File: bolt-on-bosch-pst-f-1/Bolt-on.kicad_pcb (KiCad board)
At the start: 4 copper layers, 42 x 72 mm, 12 parts

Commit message: cleanup kicad design
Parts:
- removed R_PRESS_BOT: ﻿10kΩ, Resistor_SMD:R_0805_2012Metric_Pad1.20x1.40mm_HandSolder
- removed R_PRESS_TOP: ﻿5.6kΩ, Resistor_SMD:R_0805_2012Metric_Pad1.20x1.40mm_HandSolder
- R_PRESS_BOT1, R_PRESS_TOP1: moved to B.Cu
- moved R_PRESS_BOT1 170.4 mm to (143.0, 96.5), turned to 90 degrees
- moved R_PRESS_TOP1 165.0 mm to (138.5, 96.5), turned to 90 degrees
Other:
- board text added: "5V"
- board text added: "CAN2H"
- board text added: "CAN2L"
- board text added: "GND"
- board text added: "PRESS_SIG"
- board text added: "TEMP_SIG"

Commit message: update readme
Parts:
- removed JPST-F_1_IN1: Conn_01x04, Connector_JST:JST_PH_S4B-PH-K_1x04_P2.00mm_Horizontal
- added PST-F1_IN1: Conn_01x04, Connector_JST:JST_PH_S4B-PH-K_1x04_P2.00mm_Horizontal, B.Cu at (136.5, 76.0)
- moved C2 16.0 mm to (143.5, 84.5), turned to 0 degrees
- moved C1 9.39 mm to (143.5, 88.0), turned to 0 degrees
- moved CAN2_5V1 1.50 mm to (153.5, 76.0)
- moved D1 0.71 mm to (159.0, 96.5)
- moved R_PRESS_BOT1 0.50 mm to (142.5, 96.5)
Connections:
- C1 pad 2: IO35 -> /IO35
- C2 pad 2: IO36 -> /IO36
- D1 pad 1: unconnected-(D1-Pad1) -> /IO35
- D1 pad 2: IO35 -> /IO36
- R_PRESS_BOT1 pad 1: IO35 -> /IO35
- R_PRESS_TOP1 pad 1: IO35 -> /IO35
- R_TEMP_TOP1 pad 1: IO36 -> /IO36
- SV1 pad 12: IO35 -> /IO35
- SV1 pad 13: IO36 -> /IO36
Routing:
- net /IO36: track 0.00 -> 79.0 mm
- net IO36: track 76.0 -> 0.00 mm
- net /IO35: track 0.00 -> 51.0 mm
- net IO35: track 39.9 -> 0.00 mm
- net GND: track 90.1 -> 77.6 mm
- net /+5V: track 81.0 -> 85.0 mm
- net /CAN2H: track 33.0 -> 34.9 mm
- net Net-(PST-F1_IN1-PRESS_SIG): track 18.0 -> 19.5 mm
- net /CAN2L: track 31.3 -> 30.3 mm

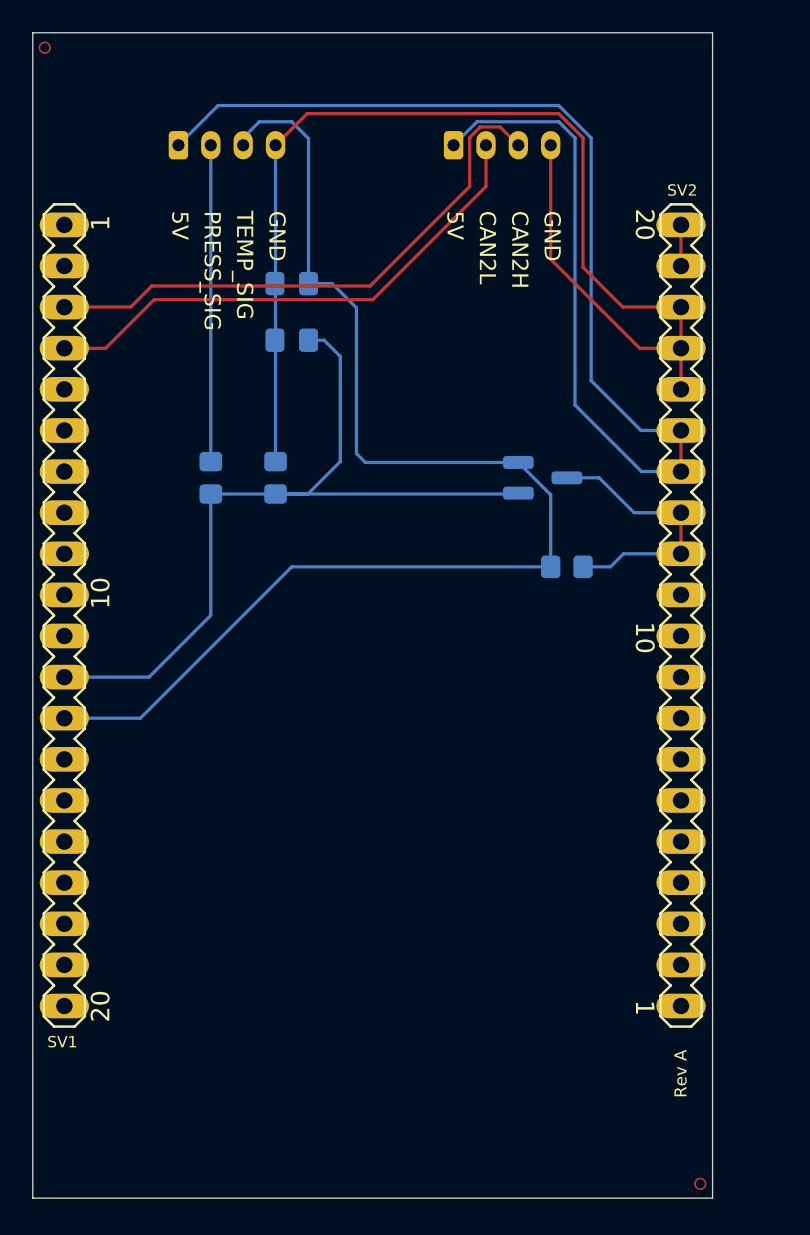
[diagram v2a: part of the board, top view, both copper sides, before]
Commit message: add copper pour to gnd and 5v
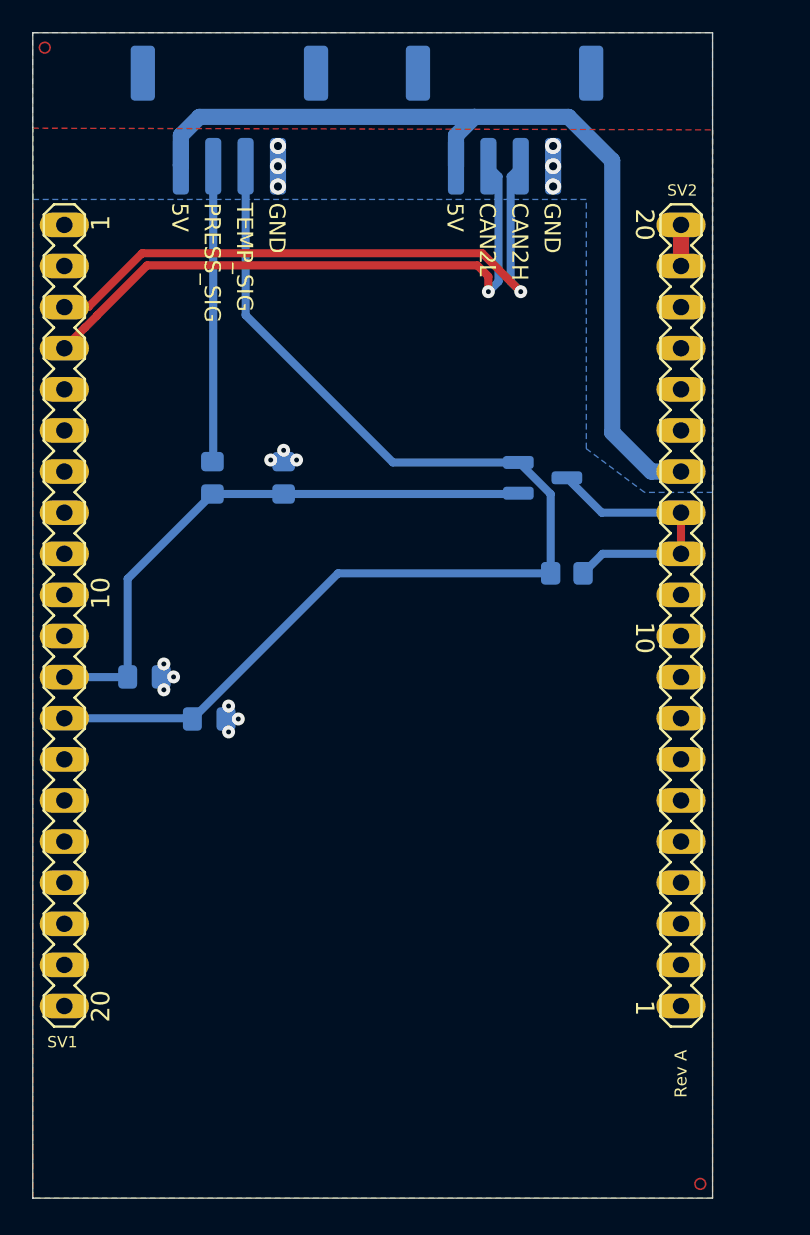
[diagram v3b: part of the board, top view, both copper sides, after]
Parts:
- CAN2_5V1, PST-F1_IN1: footprint Connector_JST:JST_PH_S4B-PH-K_1x04_P2.00mm_Horizontal -> Connector_JST:JST_PH_S4B-PH-SM4-TB_1x04-1MP_P2.00mm_Horizontal
- moved C2 27.4 mm to (138.4, 111.4), turned to 180 degrees
- moved C1 22.7 mm to (134.4, 108.8), turned to 180 degrees
- moved CAN2_5V1 3.51 mm to (156.7, 74.4)
- moved PST-F1_IN1 3.51 mm to (139.7, 74.4)
- moved R_PRESS_BOT1 0.50 mm to (143.0, 96.5)
- moved R_TEMP_TOP1 0.40 mm to (160.5, 102.4)
- moved R_PRESS_TOP1 0.10 mm to (138.6, 96.5)
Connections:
- net /CAN2H renamed /CAN2+
- net /CAN2L renamed /CAN2-
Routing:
- net GND: track 77.6 -> 0.00 mm, vias 0 -> 15
- net /+5V: track 85.0 -> 55.7 mm
- net /IO35: track 51.0 -> 36.6 mm
- net /IO36: track 79.0 -> 71.3 mm
- net /CAN2-: track 30.3 -> 37.9 mm, vias 0 -> 1
- net /CAN2+: track 34.9 -> 38.8 mm, vias 0 -> 1
- net Net-(PST-F1_IN1-PRESS_SIG): track 19.5 -> 18.3 mm
- added copper zone on B.Cu, net /+5V
- added copper zone on F.Cu, net GND

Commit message: swaped jst positions
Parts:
- added C3: ﻿0.1µF, Capacitor_SMD:C_0805_2012Metric_Pad1.18x1.45mm_HandSolder, B.Cu at (151.6, 81.5)
- added C4: 1µF, Capacitor_SMD:C_0805_2012Metric_Pad1.18x1.45mm_HandSolder, B.Cu at (148.4, 81.5)
- added C5: 10µF, Capacitor_SMD:C_1206_3216Metric_Pad1.33x1.80mm_HandSolder, B.Cu at (145.0, 81.5)
- moved CAN2_5V1 17.0 mm to (139.7, 74.1)
- moved PST-F1_IN1 17.0 mm to (156.7, 74.1)
- moved C2 4.26 mm to (134.3, 112.4)
- moved C1 1.11 mm to (134.3, 107.7)
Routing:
- net GND: track 0.00 -> 24.9 mm, vias 15 -> 8
- net /CAN2+: track 38.8 -> 23.1 mm
- net /CAN2-: track 37.9 -> 22.2 mm
- net Net-(PST-F1_IN1-PRESS_SIG): track 18.3 -> 32.7 mm
- net /IO36: track 71.3 -> 61.0 mm
- net /IO35: track 36.6 -> 35.8 mm

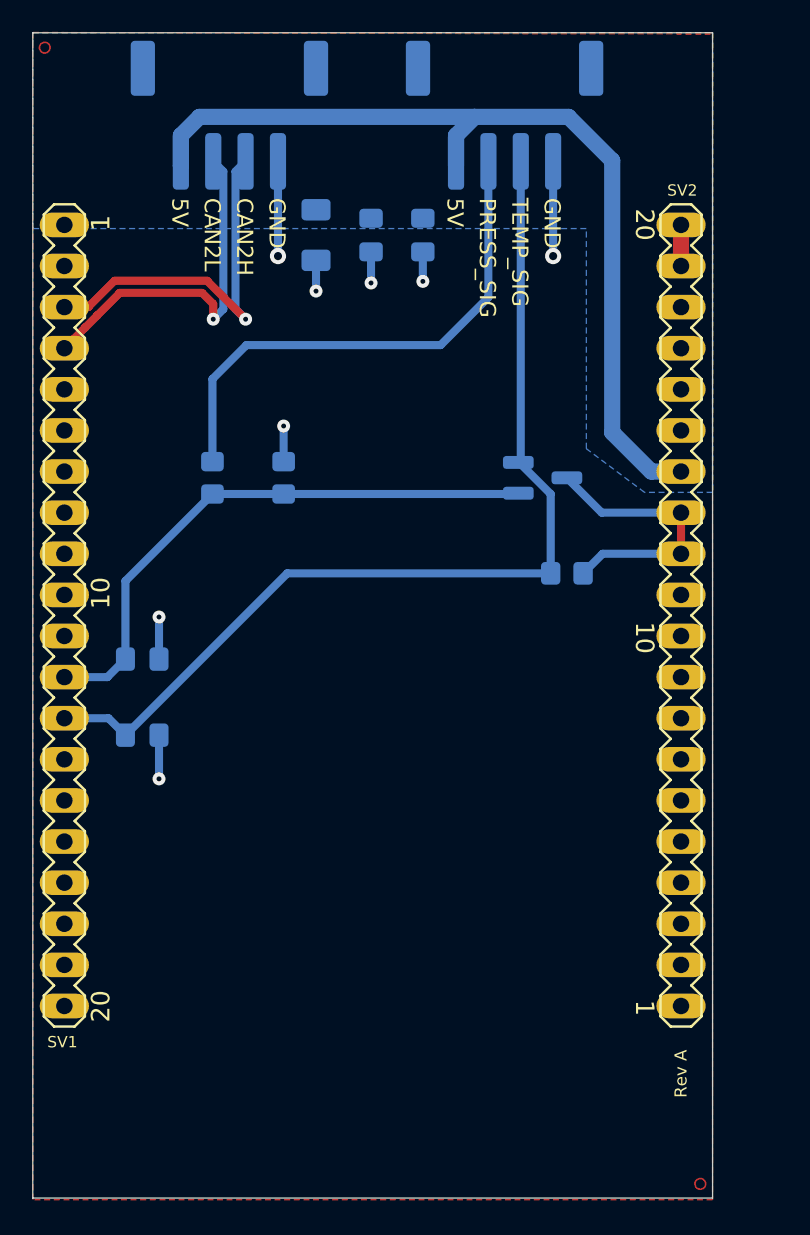
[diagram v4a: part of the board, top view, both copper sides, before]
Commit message: redo board layout
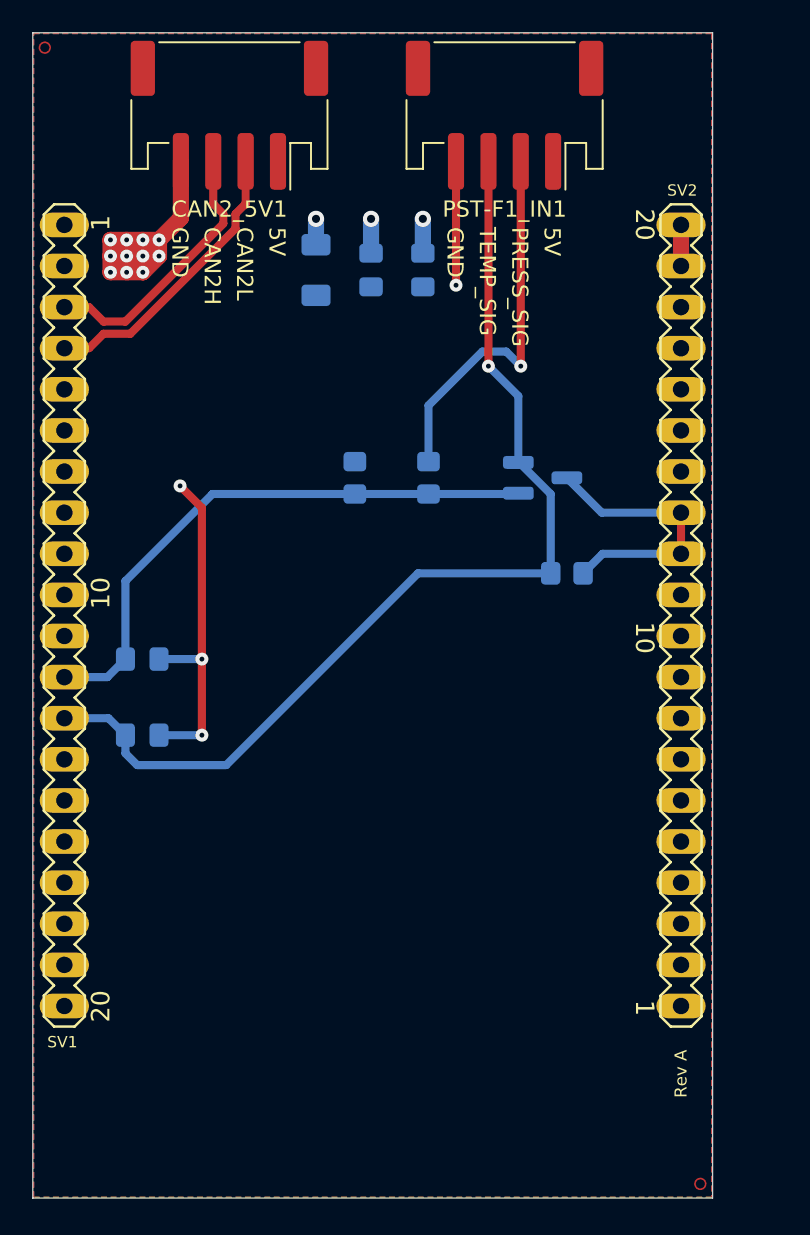
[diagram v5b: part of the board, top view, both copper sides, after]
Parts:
- CAN2_5V1, PST-F1_IN1: moved to F.Cu
- moved R_PRESS_TOP1 13.3 mm to (151.9, 96.5)
- moved R_PRESS_BOT1 4.40 mm to (147.4, 96.5)
- moved C3 2.16 mm to (151.6, 83.7)
- moved C4 2.16 mm to (148.4, 83.7)
- moved C5 2.16 mm to (145.0, 83.7)
- turned CAN2_5V1 to 180 degrees
- turned PST-F1_IN1 to 180 degrees
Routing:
- net /+5V: track 55.7 -> 5.85 mm, vias 0 -> 3
- net GND: track 24.9 -> 50.7 mm, vias 8 -> 15
- net Net-(PST-F1_IN1-PRESS_SIG): track 32.7 -> 23.6 mm, vias 0 -> 1
- net /CAN2+: track 23.1 -> 16.8 mm, vias 1 -> 0
- net /CAN2-: track 22.2 -> 18.1 mm, vias 1 -> 0
- net /IO36: track 61.0 -> 64.1 mm, vias 0 -> 1
- added copper zone on F.Cu, net /+5V
- added copper zone on B.Cu, net GND
- removed copper zone on B.Cu, net /+5V
- removed copper zone on F.Cu, net GND
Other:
- copper layers 4 -> 2

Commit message: update board layout
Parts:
- moved R_TEMP_TOP1 25.3 mm to (137.7, 113.3)
- moved D1 15.2 mm to (146.7, 105.4)
- moved R_PRESS_BOT1 12.5 mm to (137.0, 103.5)
- moved R_PRESS_TOP1 12.5 mm to (141.5, 103.5)
- moved C1 1.38 mm to (133.7, 106.4), turned to -90 degrees
- moved C2 0.55 mm to (133.7, 112.3), turned to -90 degrees
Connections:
- D1 pad 1: /IO35 -> /IO36
- D1 pad 2: /IO36 -> /IO35
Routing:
- net /+3.3V: track 17.0 -> 58.6 mm
- net /IO35: track 35.8 -> 17.5 mm
- net GND: track 50.7 -> 35.0 mm, vias 15 -> 16
- net Net-(PST-F1_IN1-PRESS_SIG): track 23.6 -> 37.7 mm
- net /IO36: track 64.1 -> 56.1 mm

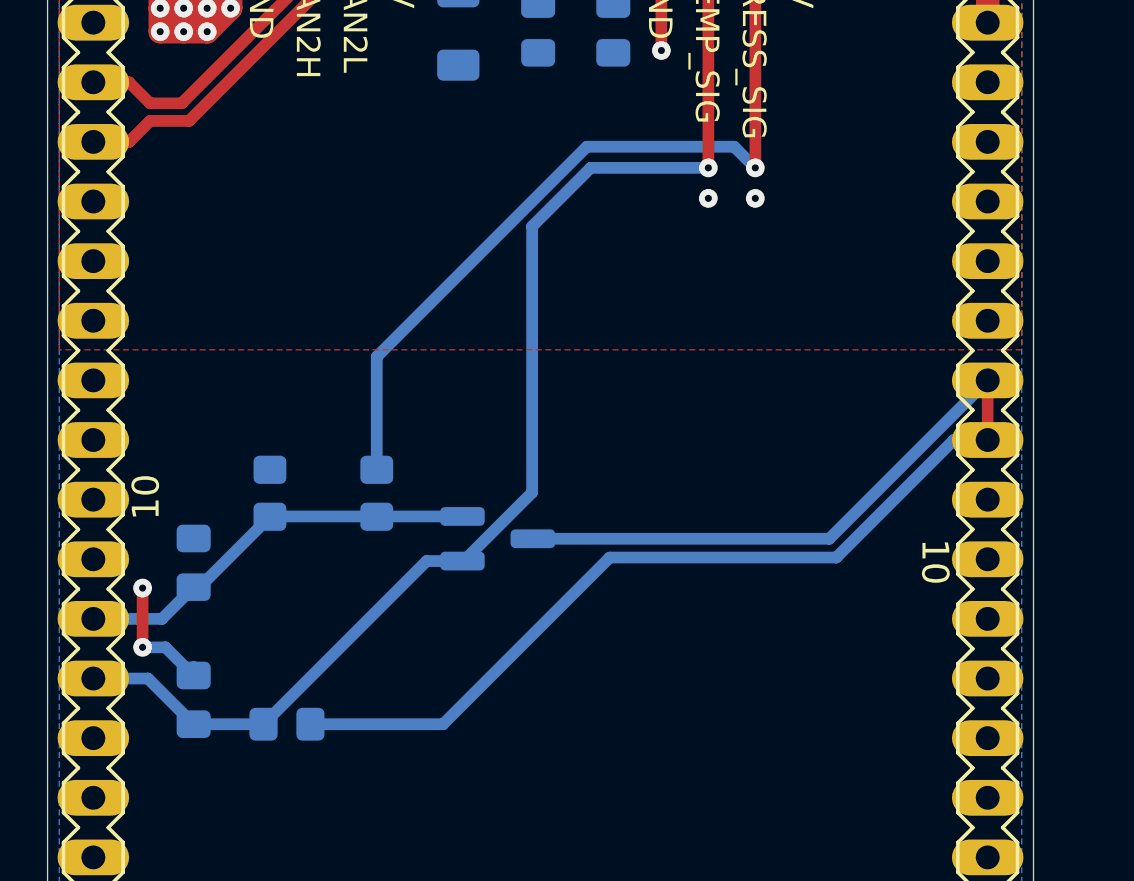
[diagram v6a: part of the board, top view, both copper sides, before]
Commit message: added low diode for proper clamp
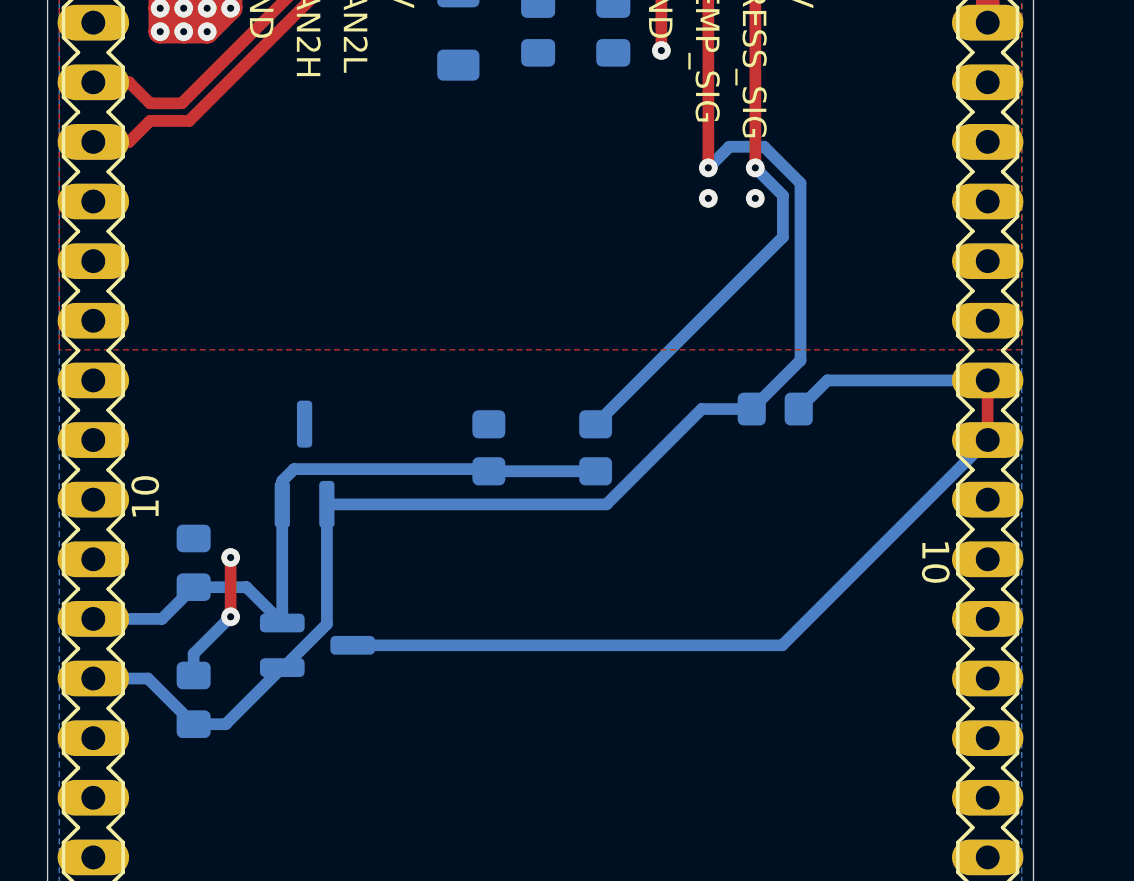
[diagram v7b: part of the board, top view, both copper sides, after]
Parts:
- added D2: BAT54A, Package_TO_SOT_SMD:TSOT-23_HandSoldering, B.Cu at (138.4, 102.2)
- moved R_TEMP_TOP1 24.8 mm to (158.5, 99.9)
- moved R_PRESS_BOT1 9.52 mm to (146.3, 101.5)
- moved R_PRESS_TOP1 9.52 mm to (150.8, 101.5)
- moved D1 8.92 mm to (139.0, 109.9)
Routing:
- net /+3.3V: track 58.6 -> 41.8 mm
- net /IO35: track 17.5 -> 29.2 mm
- net Net-(PST-F1_IN1-PRESS_SIG): track 37.7 -> 27.4 mm
- net /IO36: track 56.1 -> 65.4 mm

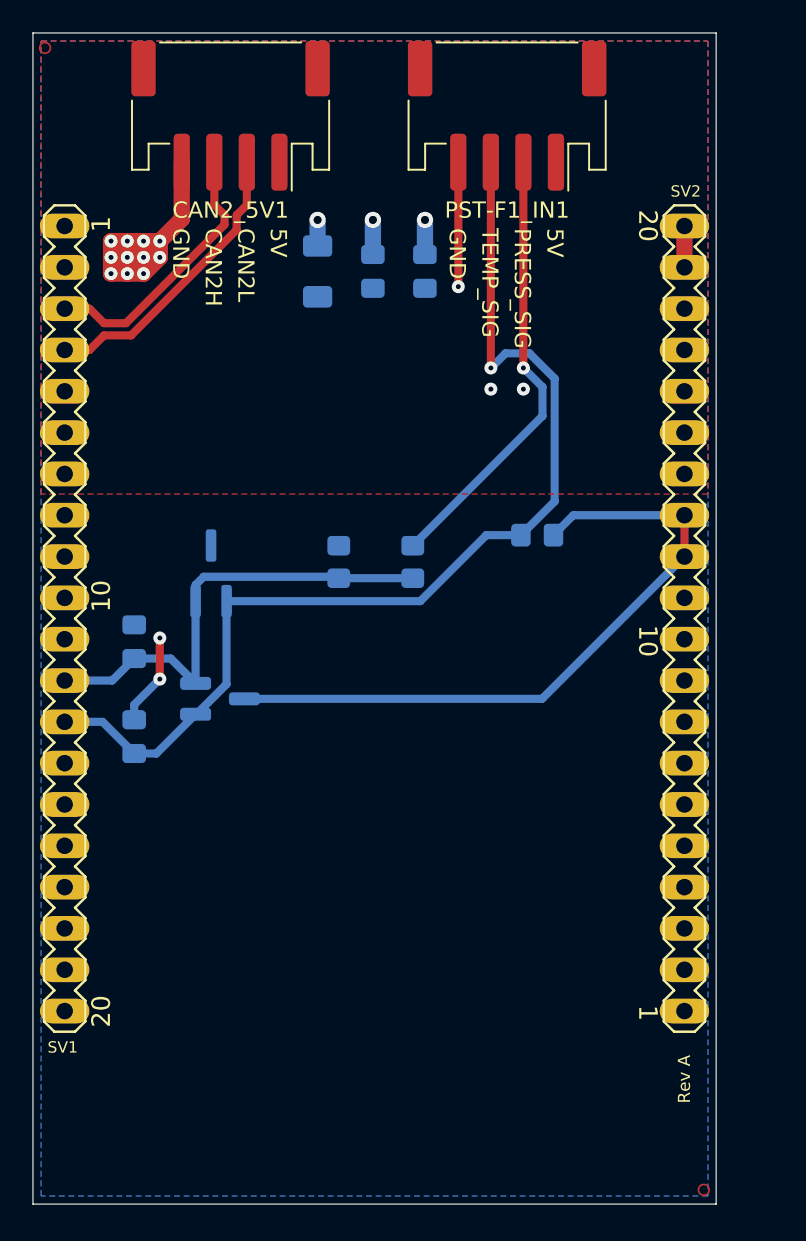
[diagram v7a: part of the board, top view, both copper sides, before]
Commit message: pcb add ground copper pour on both sides
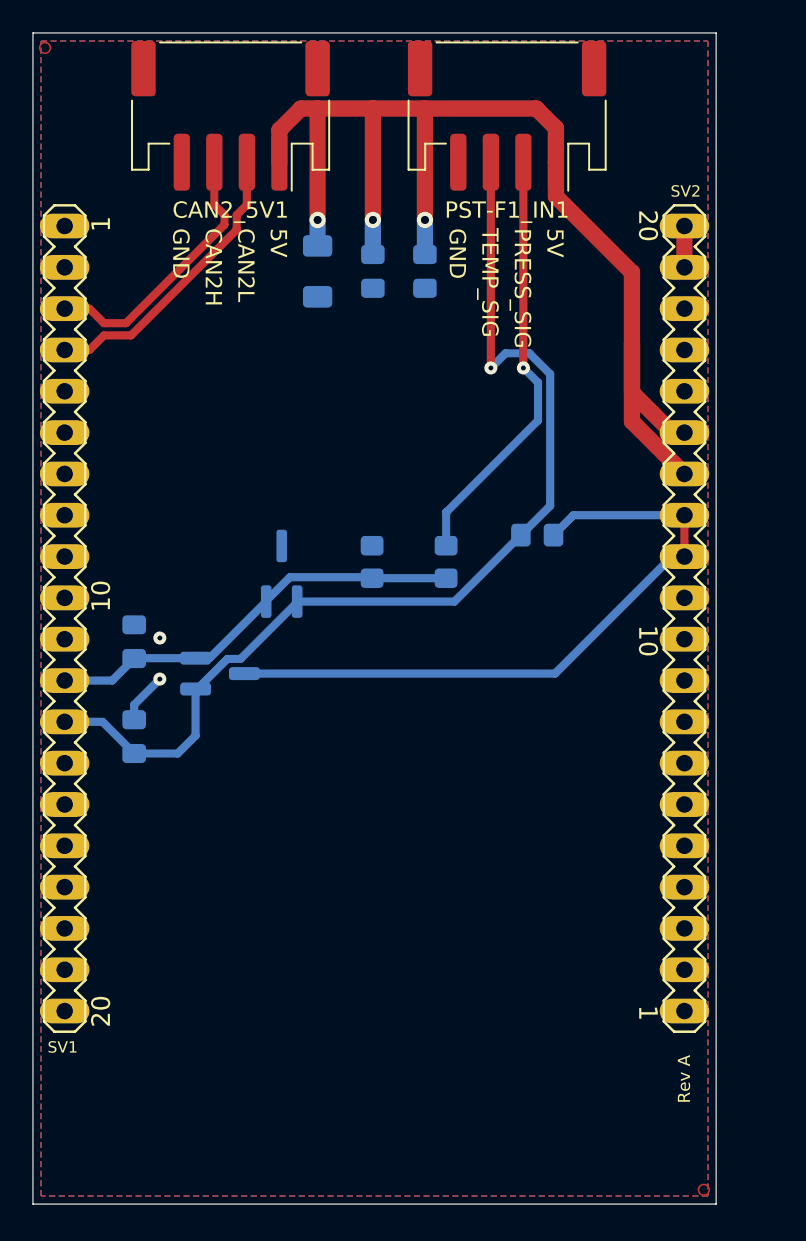
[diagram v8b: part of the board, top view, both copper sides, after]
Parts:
- moved D2 4.34 mm to (142.8, 102.2)
- moved R_PRESS_TOP1 2.05 mm to (152.9, 101.5)
- moved R_PRESS_BOT1 2.05 mm to (148.3, 101.5)
- moved D1 1.55 mm to (139.0, 108.4)
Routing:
- net /+5V: track 5.85 -> 78.2 mm
- net GND: track 35.2 -> 3.15 mm, vias 16 -> 2
- net /IO35: track 29.2 -> 26.1 mm
- net /IO36: track 65.4 -> 64.3 mm
- net Net-(PST-F1_IN1-PRESS_SIG): track 27.4 -> 26.3 mm
- net /+3.3V: track 41.8 -> 41.1 mm
- added copper zone on F.Cu, net GND
- removed copper zone on F.Cu, net /+5V
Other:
- board text added: "{ "ViaStitching": "0.2", "stitch_zone_0": { "HSpacing": "10", "VSpacing": "10", "HOffset": "0", "VOffset": "0", "Clearance": "0", "Randomize": false } }"
